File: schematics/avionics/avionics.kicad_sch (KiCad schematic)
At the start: 15 parts, among them SW1 SW_SPST, SW2 SW_DPST, SW3 SW_SPST, SW4 SW_SPST, SW5 SW_DPST, U1 TeleMega

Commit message: updated av bay schematic
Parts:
- removed BT1: 3.7V LIPO, symbol Device:Battery
- removed BT3: 4.1V LIPO, symbol Device:Battery
- removed R1, R2, R3, R4: R_ignite, symbol recovery:R_Igniter
- removed SW1, SW3, SW4: SW_SPST, symbol Switch:SW_SPST
- removed SW2, SW5: SW_DPST, symbol Switch:SW_DPST
- removed U1: TeleMega, symbol altusmetrum:telemega
- removed U2: ~, symbol featherweight:blue_raven
- removed U3: ~, symbol featherweight:tracker_gps
- added BT5, BT6: 4.1V LIPO, symbol Device:Battery
- added J1, J5: Barrier_Block_3C6W, symbol Connector_Generic:Conn_02x03_Top_Bottom
- added J3, J4, J6, J7: Barrier_Block_2C4W, symbol Connector_Generic:Conn_02x02_Top_Bottom
- added R5, R6, R8, R9: R_ignite, symbol recovery:R_Igniter
- added SW11, SW7: SW_DPST, symbol Switch:SW_DPST
- added SW6, SW8, SW9: SW_SPST, symbol Switch:SW_SPST
- added U2: TeleMega, symbol altusmetrum:telemega
- added U4: ~, symbol featherweight:blue_raven
- added U5: ~, symbol featherweight:tracker_gps
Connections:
- net at BT2.1 (+): now also U2.2 (BAT+)
- net at BT2.2 (-): now also U2.1 (BAT-)
- new net: BT5.1 (+), SW6.2 (B)
- new net: BT5.2 (-), J1.5 (Pin_5)
- new net: SW7.1, U4.3 (APO)
- new net: J3.1 (Pin_1), SW7.2
- new net: SW7.3, U4.4 (MAIN)
- new net: J4.1 (Pin_1), SW7.4
- new net: J3.2 (Pin_2), J4.2 (Pin_2), J5.6 (Pin_6)
- new net: J4.3 (Pin_3), R6.1
- new net: J4.4 (Pin_4), R6.2
- new net: SW9.1 (A), U2.2 (BAT+)
- new net: SW9.2 (B), U2.1 (BAT-)
- new net: J6.1 (Pin_1), SW11.2
- new net: J6.2 (Pin_2), U2.6 (APO-)
- new net: J6.3 (Pin_3), R8.1
- new net: J6.4 (Pin_4), R8.2
- new net: J5.1 (Pin_1), U4.1 (+)
- new net: J5.2 (Pin_2), J5.3 (Pin_3), U4.2 (GND)
- new net: J5.4 (Pin_4), SW8.1 (A)
- new net: BT6.2 (-), J1.4 (Pin_4), J5.5 (Pin_5)
- new net: J7.3 (Pin_3), R9.1
- new net: J7.4 (Pin_4), R9.2
- new net: BT6.1 (+), SW8.2 (B)
- new net: J3.3 (Pin_3), R5.1
- new net: J3.4 (Pin_4), R5.2
- new net: SW11.1, U2.7 (APO+)
- new net: SW11.3, U2.5 (MAIN+)
- new net: J7.1 (Pin_1), SW11.4
- new net: J1.1 (Pin_1), J1.2 (Pin_2), U5.1 (-)
- new net: J1.3 (Pin_3), U5.2 (+)
- new net: J7.2 (Pin_2), U2.4 (MAIN-)
- new net: J1.6 (Pin_6), SW6.1 (A)
- new net: U2.11 (PYRO), U2.12 (LIPO)
- no-connect marks 11 -> 12
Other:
- company: (none) -> WE Rocketry
- title: (none) -> Hyperion2 Avionics Bay Wiring

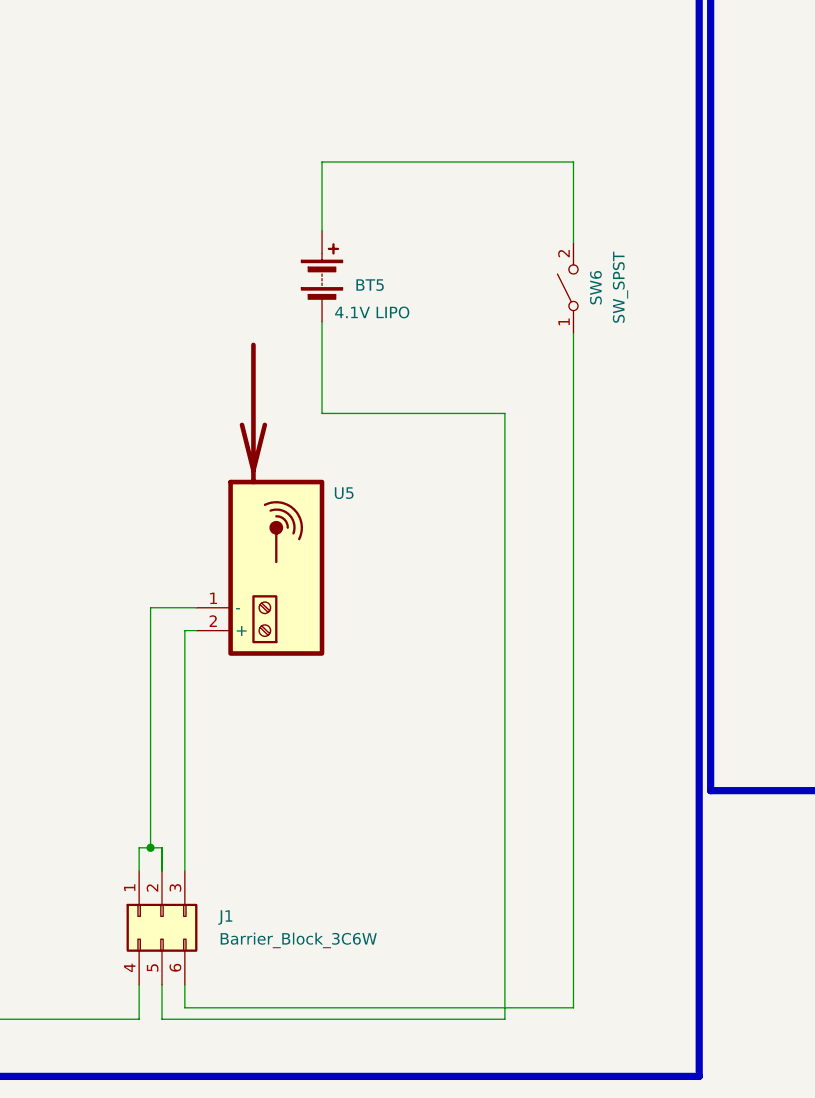
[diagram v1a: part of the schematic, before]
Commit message: fixed schem switch
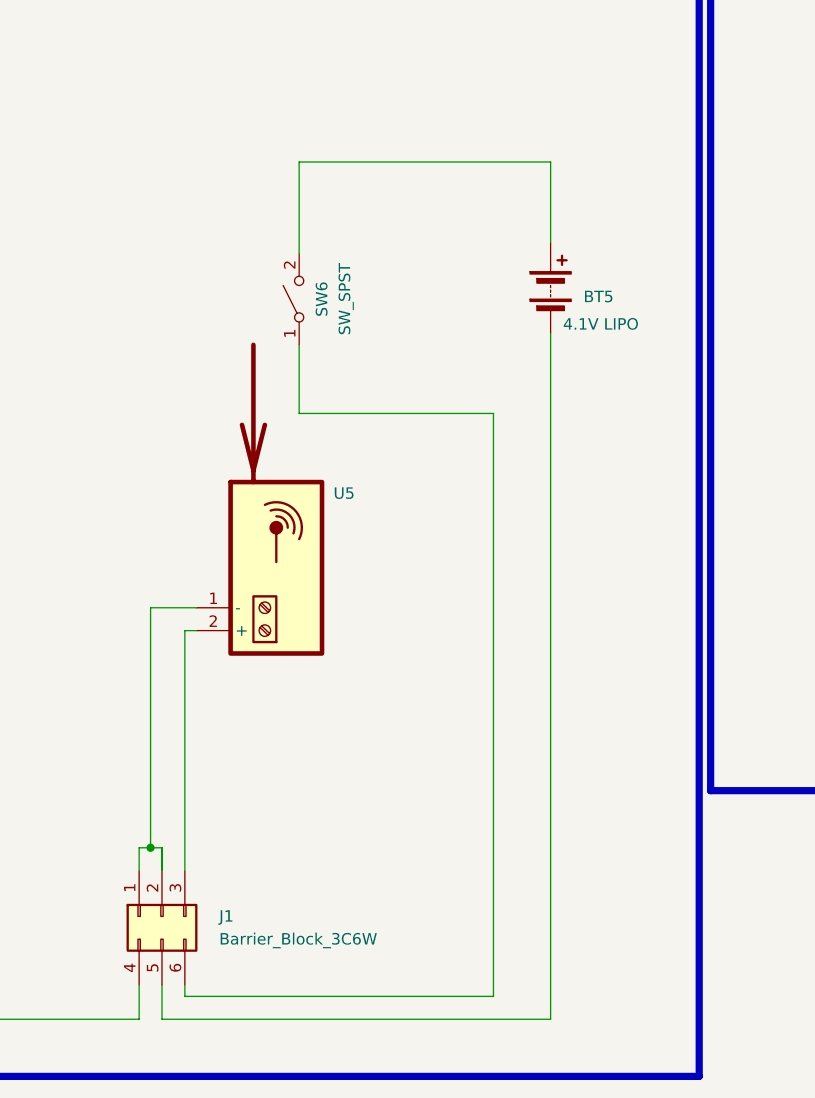
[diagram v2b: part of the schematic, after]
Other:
- moved on the sheet: BT5, SW6
